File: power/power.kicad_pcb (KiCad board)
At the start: 4 copper layers, 75 x 56 mm, 66 parts, among them J1 GPIO, J10 SCL1, J11 SDA1, J12 SCL2, J13 SDA2, J14 VCC1, J15 GND1, J16 VCC2, J17 GND2, J18 JP_VCC_PWM, J19 Conn_01x01, J2 PWM_OUT, J3 PWM_IN, J4 JP_EXT, J5 JP_VOLTS, J6 I2C_EXT1, J7 I2C_EXT2, J8 PWM_OUT, J9 JP_VCC_PWM, Q1 D15P05, Q2 BC847C, U2 REF5050IDGK, U3 L78L06_SOT89, U5 TPS56A37RPAR

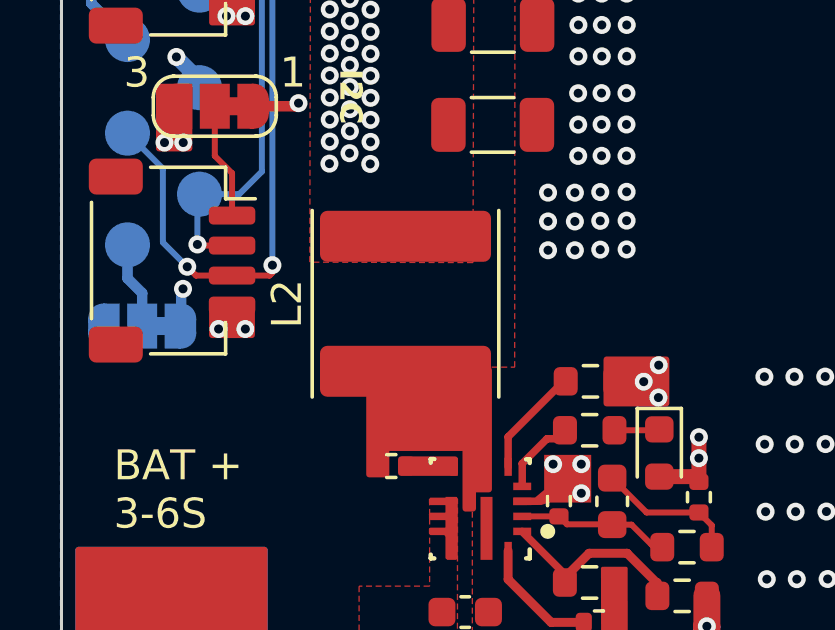
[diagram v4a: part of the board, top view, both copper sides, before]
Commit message: add custom inductor footprint
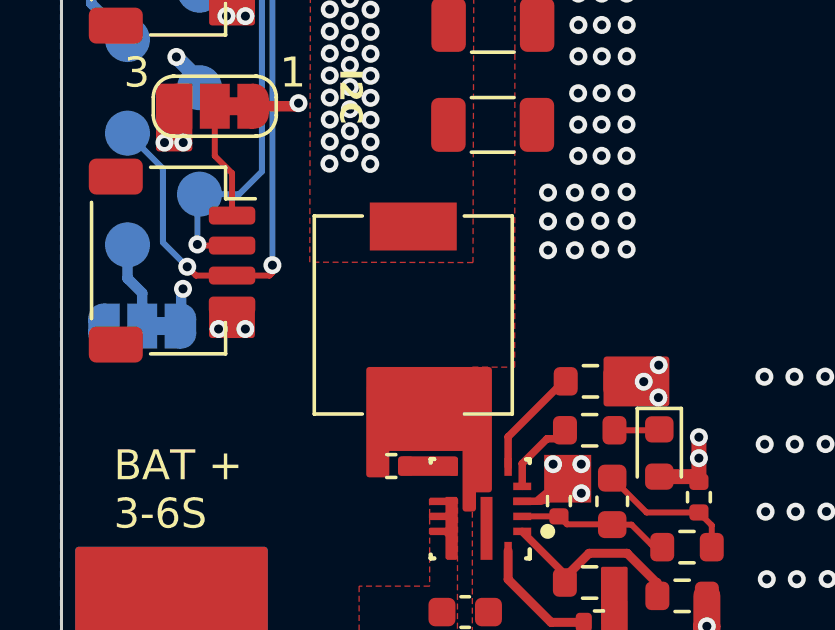
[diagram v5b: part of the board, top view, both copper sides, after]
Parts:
- L2: footprint Inductor_SMD:L_Sunlord_SWPA6045S -> pilotpi:L_6.6x7.5_H4
- moved L2 0.45 mm to (111.7, 69.8)
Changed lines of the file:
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@@
 		)
 	)
-	(footprint "Inductor_SMD:L_Sunlord_SWPA6045S"
+	(footprint "pilotpi:L_6.6x7.5_H4"
 		(layer "F.Cu")
-		(at 111.466844 69.437848 90)
-		(descr "Inductor, Sunlord, SWPA6045S, 6.0x6.0x4.5mm, (https://www.sunlordinc.com/UploadFiles/PDF_Cat/20120704094224784.pdf)")
-		(tags "swpa")
+		(at 111.726498 69.811381 90)
+		(descr "Choke, SMD, 6.3x6.3mm 3mm height")
+		(tags "Choke SMD")
 		(property "Reference" "L2"
-			(at 0 -3.95 90)
-			(layer "F.SilkS")
+			(at 0 -4.45 90)
+			(layer "F.SilkS")
+			(hide yes)
 			(effects
 				(font
@@
 		)
 		(property "Value" "3.3uH 16A 6.5mΩ ±20%"
-			(at 0 3.95 90)
+			(at 0 4.45 90)
 			(layer "F.Fab")
 			(effects
@@
 		(property "Datasheet" ""
 			(at 0 0 90)
+			(unlocked yes)
 			(layer "F.Fab")
 			(hide yes)
@@
 				(font
 					(size 1.27 1.27)
+					(thickness 0.15)
 				)
 			)
@@
 		(property "Description" "I_peak = 11.25A, I_rms = 10.03A"
 			(at 0 0 90)
+			(unlocked yes)
 			(layer "F.Fab")
 			(hide yes)
@@
 				(font
 					(size 1.27 1.27)
-				)
-			)
-		)
-		(property "KiLib_Generator" "inductor/SMD"
-			(at 0 0 90)
-			(layer "F.SilkS")
-			(hide yes)
-			(effects
-				(font
-					(size 1 1)
 					(thickness 0.15)
 				)
@@
 		(duplicate_pad_numbers_are_jumpers no)
 		(fp_line
-			(start -3.11 -3.11)
-			(end 3.11 -3.11)
-			(stroke
-				(width 0.12)
-				(type solid)
-			)
-			(layer "F.SilkS")
-		)
-		(fp_line
-			(start 3.11 3.11)
-			(end -3.11 3.11)
-			(stroke
-				(width 0.12)
-				(type solid)
-			)
-			(layer "F.SilkS")
-		)
-		(fp_line
-			(start 3.25 -3.25)
-			(end 3.25 -3.1)
-			(stroke
-				(width 0.05)
-				(type solid)
-			)
-			(layer "F.CrtYd")
-		)
-		(fp_line
-			(start -3.25 -3.25)
-			(end 3.25 -3.25)
-			(stroke
-				(width 0.05)
-				(type solid)
-			)
-			(layer "F.CrtYd")
-		)
-		(fp_line
-			(start 3.35 -3.1)
-			(end 3.35 3.1)
-			(stroke
-				(width 0.05)
-				(type solid)
-			)
-			(layer "F.CrtYd")
-		)
-		(fp_line
-			(start 3.25 -3.1)
-			(end 3.35 -3.1)
-			(stroke
-				(width 0.05)
-				(type solid)
-			)
-			(layer "F.CrtYd")
-		)
-		(fp_line
-			(start -3.25 -3.1)
-			(end -3.25 -3.25)
-			(stroke
-				(width 0.05)
-				(type solid)
-			)
-			(layer "F.CrtYd")
-		)
-		(fp_line
-			(start -3.35 -3.1)
-			(end -3.25 -3.1)
-			(stroke
-				(width 0.05)
-				(type solid)
-			)
-			(layer "F.CrtYd")
-		)
-		(fp_line
-			(start 3.35 3.1)
-			(end 3.25 3.1)
-			(stroke
-				(width 0.05)
-				(type solid)
-			)
-			(layer "F.CrtYd")
-		)
-		(fp_line
-			(start 3.25 3.1)
-			(end 3.25 3.25)
-			(stroke
-				(width 0.05)
-				(type solid)
-			)
-			(layer "F.CrtYd")
-		)
-		(fp_line
-			(start -3.25 3.1)
-			(end -3.35 3.1)
-			(stroke
-				(width 0.05)
-				(type solid)
-			)
-			(layer "F.CrtYd")
-		)
-		(fp_line
-			(start -3.35 3.1)
-			(end -3.35 -3.1)
-			(stroke
-				(width 0.05)
-				(type solid)
-			)
-			(layer "F.CrtYd")
-		)
-		(fp_line
-			(start 3.25 3.25)
-			(end -3.25 3.25)
-			(stroke
-				(width 0.05)
-				(type solid)
-			)
-			(layer "F.CrtYd")
-		)
-		(fp_line
-			(start -3.25 3.25)
-			(end -3.25 3.1)
-			(stroke
-				(width 0.05)
-				(type solid)
-			)
-			(layer "F.CrtYd")
-		)
-		(fp_rect
-			(start -3 -3)
-			(end 3 3)
-			(stroke
-				(width 0.1)
-				(type solid)
-			)
-			(fill no)
+			(start 3.3 -3.3)
+			(end 3.3 -1.7)
+			(stroke
+				(width 0.12)
+				(type solid)
+			)
+			(layer "F.SilkS")
+		)
+		(fp_line
+			(start -3.3 -3.3)
+			(end 3.3 -3.3)
+			(stroke
+				(width 0.12)
+				(type solid)
+			)
+			(layer "F.SilkS")
+		)
+		(fp_line
+			(start -3.3 -1.7)
+			(end -3.3 -3.3)
+			(stroke
+				(width 0.12)
+				(type solid)
+			)
+			(layer "F.SilkS")
+		)
+		(fp_line
+			(start 3.3 1.7)
+			(end 3.3 3.3)
+			(stroke
+				(width 0.12)
+				(type solid)
+			)
+			(layer "F.SilkS")
+		)
+		(fp_line
+			(start 3.3 3.3)
+			(end -3.3 3.3)
+			(stroke
+				(width 0.12)
+				(type solid)
+			)
+			(layer "F.SilkS")
+		)
+		(fp_line
+			(start -3.3 3.3)
+			(end -3.3 1.7)
+			(stroke
+				(width 0.12)
+				(type solid)
+			)
+			(layer "F.SilkS")
+		)
+		(fp_line
+			(start 3.75 -3.4)
+			(end -3.75 -3.4)
+			(stroke
+				(width 0.05)
+				(type solid)
+			)
+			(layer "F.CrtYd")
+		)
+		(fp_line
+			(start -3.75 -3.4)
+			(end -3.75 3.4)
+			(stroke
+				(width 0.05)
+				(type solid)
+			)
+			(layer "F.CrtYd")
+		)
+		(fp_line
+			(start 3.75 3.4)
+			(end 3.75 -3.4)
+			(stroke
+				(width 0.05)
+				(type solid)
+			)
+			(layer "F.CrtYd")
+		)
+		(fp_line
+			(start -3.75 3.4)
+			(end 3.75 3.4)
+			(stroke
+				(width 0.05)
+				(type solid)
+			)
+			(layer "F.CrtYd")
+		)
+		(fp_line
+			(start 3.15 -3.15)
+			(end 3.15 -1.5)
+			(stroke
+				(width 0.1)
+				(type solid)
+			)
+			(layer "F.Fab")
+		)
+		(fp_line
+			(start -3.15 -3.15)
+			(end 3.15 -3.15)
+			(stroke
+				(width 0.1)
+				(type solid)
+			)
+			(layer "F.Fab")
+		)
+		(fp_line
+			(start -3.15 -3.15)
+			(end -3.15 -1.5)
+			(stroke
+				(width 0.1)
+				(type solid)
+			)
+			(layer "F.Fab")
+		)
+		(fp_line
+			(start 3.15 3.15)
+			(end 3.15 1.5)
+			(stroke
+				(width 0.1)
+				(type solid)
+			)
+			(layer "F.Fab")
+		)
+		(fp_line
+			(start -3.15 3.15)
+			(end -3.15 1.5)
+			(stroke
+				(width 0.1)
+				(type solid)
+			)
+			(layer "F.Fab")
+		)
+		(fp_line
+			(start -3.15 3.15)
+			(end 3.15 3.15)
+			(stroke
+				(width 0.1)
+				(type solid)
+			)
+			(layer "F.Fab")
+		)
+		(fp_arc
+			(start -1.91 -1.91)
+			(mid 0 -2.701148)
+			(end 1.91 -1.91)
+			(stroke
+				(width 0.1)
+				(type solid)
+			)
+			(layer "F.Fab")
+		)
+		(fp_arc
+			(start 1.91 1.91)
+			(mid 0 2.701148)
+			(end -1.91 1.91)
+			(stroke
+				(width 0.1)
+				(type solid)
+			)
 			(layer "F.Fab")
 		)
@@
 			)
 		)
-		(pad "1" smd roundrect
-			(at -2.25 0 90)
-			(size 1.7 5.7)
+		(pad "1" smd rect
+			(at -2.95 0 90)
+			(size 1.6 2.9)
 			(layers "F.Cu" "F.Mask" "F.Paste")
-			(roundrect_rratio 0.147059)
 			(net "Net-(U5-SW)")
 			(pinfunction "1_1")
 			(pintype "passive")
 		)
-		(pad "2" smd roundrect
-			(at 2.25 0 90)
-			(size 1.7 5.7)
+		(pad "2" smd rect
+			(at 2.95 0 90)
+			(size 1.6 2.9)
 			(layers "F.Cu" "F.Mask" "F.Paste")
-			(roundrect_rratio 0.147059)
 			(net "+5V")
 			(pinfunction "2_2")
@@
 		)
 		(embedded_fonts no)
-		(model "${KICAD10_3DMODEL_DIR}/Inductor_SMD.3dshapes/L_Sunlord_SWPA6045S.step"
+		(model "${KICAD10_3DMODEL_DIR}/Inductor_SMD.3dshapes/L_6.3x6.3_H3.step"
 			(offset
 				(xyz 0 0 0)

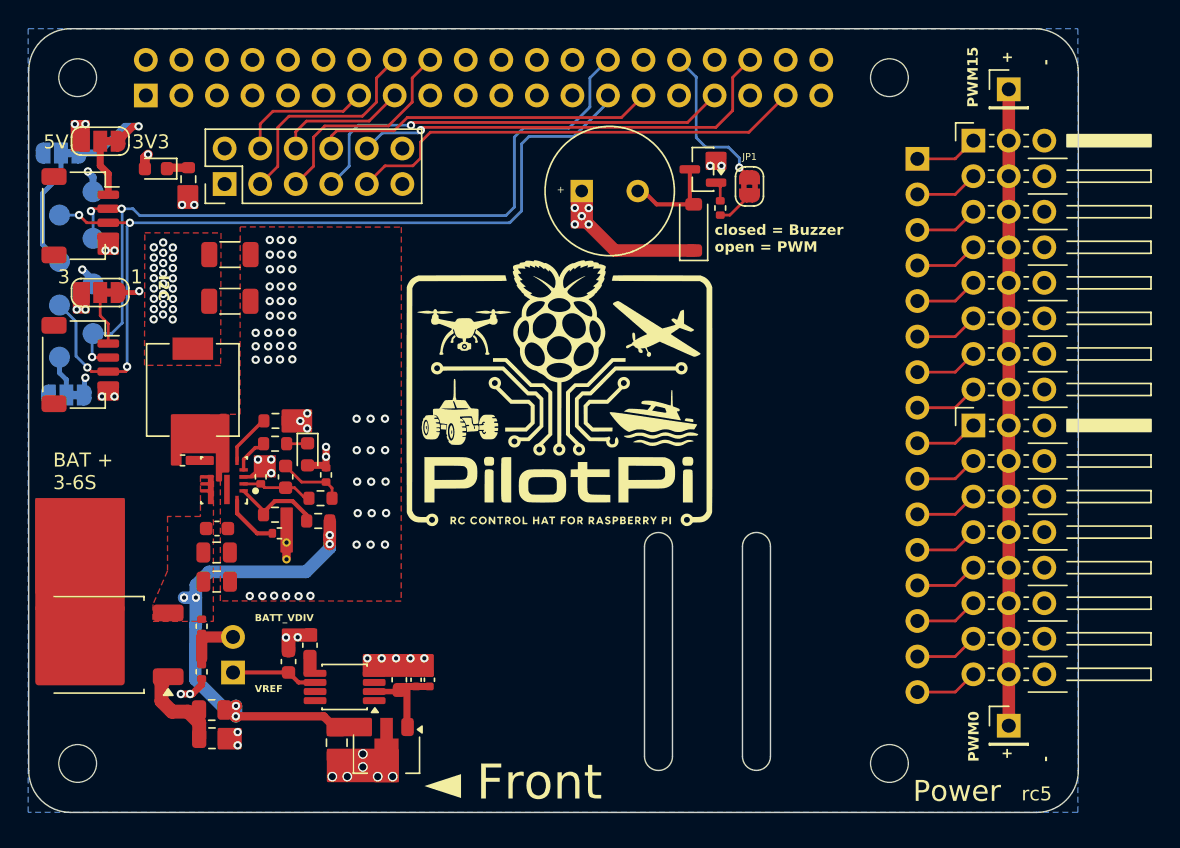
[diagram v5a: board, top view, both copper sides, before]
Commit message: added RGB indicator LED w/LP5562; added I2C pullups
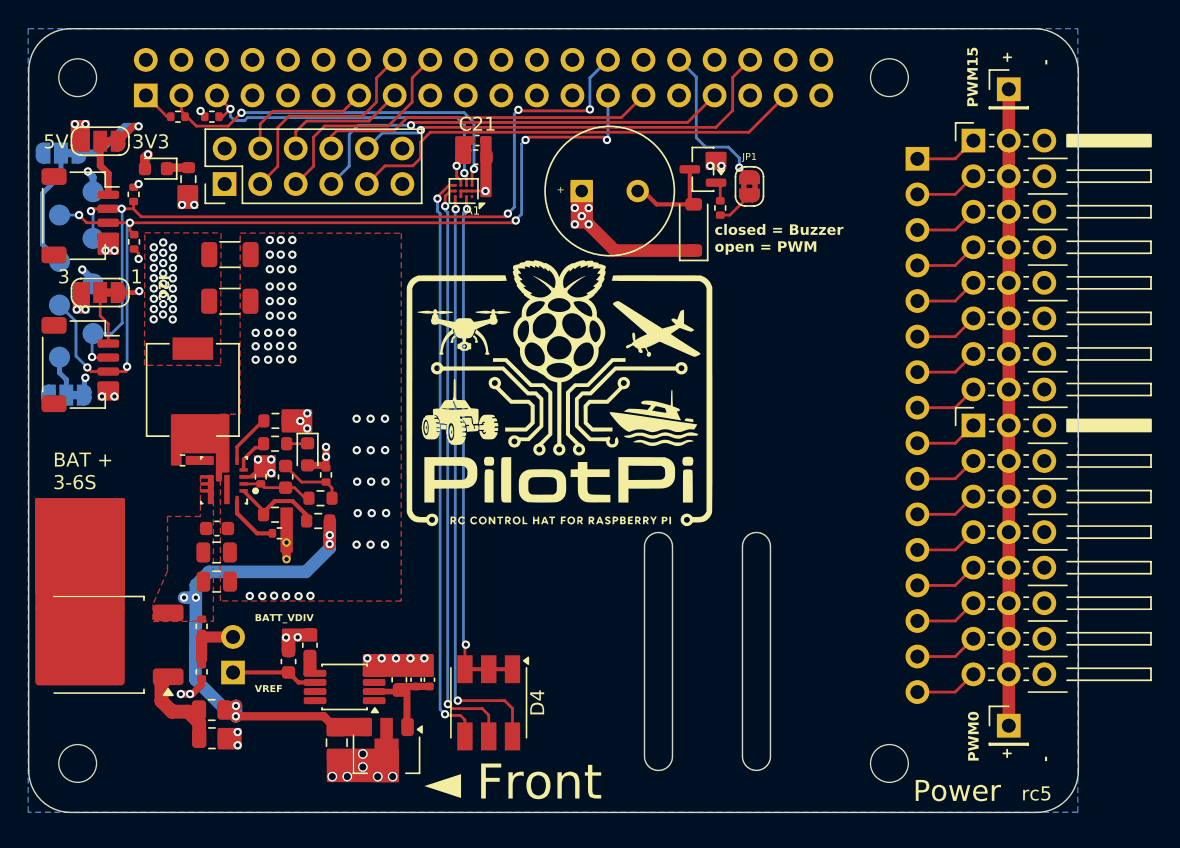
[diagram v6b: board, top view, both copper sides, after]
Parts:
- added C21: 100nF (104) 10% 16V, Capacitor_SMD:C_0402_1005Metric, F.Cu at (132.1, 52.0)
- added C22: 1uF (105) 10% 50V, Capacitor_SMD:C_0603_1608Metric, F.Cu at (131.9, 53.2)
- added D4: LED_RGB, LED_SMD:LED_RGB_5050-6, F.Cu at (132.9, 92.2)
- added R33: 3.3KΩ ±1%, Resistor_SMD:R_0402_1005Metric, F.Cu at (107.5, 59.2)
- added R34: 3.3KΩ ±1%, Resistor_SMD:R_0402_1005Metric, F.Cu at (107.5, 55.8)
- added R35: 3.3KΩ ±1%, Resistor_SMD:R_0402_1005Metric, F.Cu at (110.7, 50.3)
- added R36: 3.3KΩ ±1%, Resistor_SMD:R_0402_1005Metric, F.Cu at (113.1, 50.3)
- added U1: LP5562, pilotpi:Texas_DSBGA-12_1.648x1.248mm_Layout3x4_P0.4mm, F.Cu at (131.1, 55.6)
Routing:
- net +3V3: track 60.7 -> 117.7 mm, vias 3 -> 9
- net Net-(D4-RA): track 0.00 -> 42.2 mm, vias 0 -> 2
- net Net-(D4-GA): track 0.00 -> 42.0 mm, vias 0 -> 2
- net Net-(D4-BA): track 0.00 -> 41.6 mm, vias 0 -> 2
- net /GPIO2/SDA1: track 0.00 -> 27.7 mm, vias 0 -> 2
- net /GPIO3/SCL1: track 0.00 -> 24.5 mm, vias 0 -> 2
- net /GPIO0/SDA0: track 64.8 -> 68.2 mm, vias 4 -> 7
- net GND: track 5.56 -> 7.72 mm, vias 78 -> 79
- net /GPIO1/SCL0: track 61.8 -> 63.5 mm, vias 3 -> 6

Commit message: change UVLO network Better protect against reverse current outrush when disconnecting the battery with external 5V supply connected. -> VSTART=7.96V, VSTOP=7.16, hysteresis=797mV (s. https://www.ti.com/lit/ds/symlink/tps56a37.pdf?ts=1779344700851 Chapter 6.3.6)
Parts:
- R13: value 169kΩ / 1% -> 17.8kΩ / 1%
- R14: value 36.1kΩ / 1% -> 3.09kΩ / 1%
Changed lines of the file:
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@@
 			)
 		)
-		(property "Value" "169kΩ / 1%"
+		(property "Value" "17.8kΩ / 1%"
 			(at 0 1.43 0)
 			(layer "F.Fab")
@@
 			)
 		)
-		(property "Part" "0603WAF1693T5E"
+		(property "Part" "PTFR0402B17K8N9"
 			(at 0 0 0)
 			(unlocked yes)
@@
 			)
 		)
-		(property "Value" "36.1kΩ / 1%"
+		(property "Value" "3.09kΩ / 1%"
 			(at 0 1.43 0)
 			(layer "F.Fab")
@@
 			)
 		)
-		(property "Part" "RT0603BRD0736K1L"
+		(property "Part" "FRC0603F3091TS"
 			(at 0 0 0)
 			(unlocked yes)

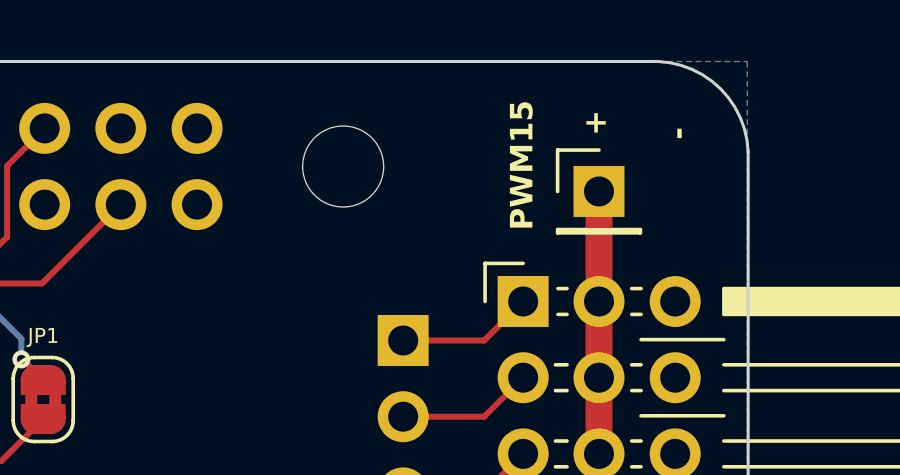
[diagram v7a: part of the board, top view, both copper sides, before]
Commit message: add 5V pin pad near PWM VCC input pin
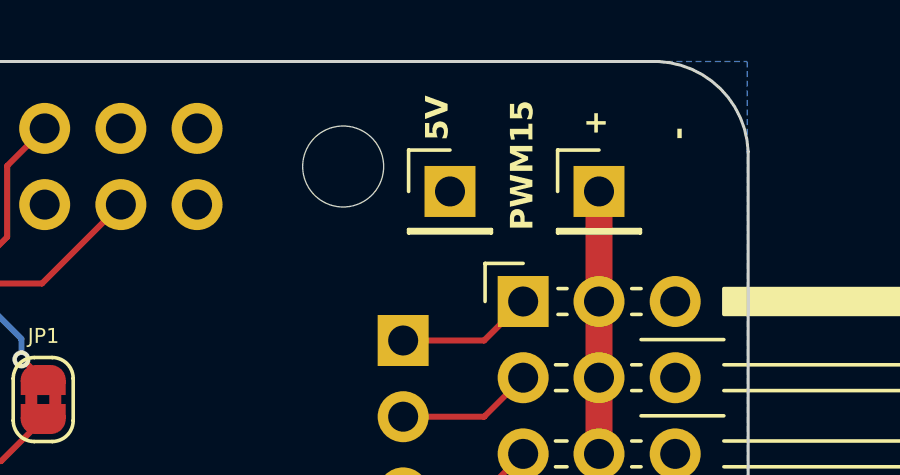
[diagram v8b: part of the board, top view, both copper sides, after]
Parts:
- added J20: JP_VCC_PWM, Connector_PinHeader_2.54mm:PinHeader_1x01_P2.54mm_Vertical, F.Cu at (165.1, 48.3)
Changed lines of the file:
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@@
 		)
 	)
+	(footprint "Connector_PinHeader_2.54mm:PinHeader_1x01_P2.54mm_Vertical"
+		(layer "F.Cu")
+		(at 165.061167 48.332007)
+		(descr "Through hole straight pin header, 1x01, 2.54mm pitch, single row")
+		(tags "Through hole pin header THT 1x01 2.54mm single row")
+		(property "Reference" "J20"
+			(at 0 -2.38 0)
+			(layer "F.SilkS")
+			(hide yes)
+			(effects
+				(font
+					(size 1 1)
+					(thickness 0.15)
+				)
+			)
+		)
+		(property "Value" "JP_VCC_PWM"
+			(at 0 2.38 0)
+			(layer "F.Fab")
+			(effects
+				(font
+					(size 1 1)
+					(thickness 0.15)
+				)
+			)
+		)
+		(property "Datasheet" ""
+			(at 0 0 0)
+			(layer "F.Fab")
+			(hide yes)
+			(effects
+				(font
+					(size 1.27 1.27)
+				)
+			)
+		)
+		(property "Description" "Generic connector, single row, 01x01, script generated (kicad-library-utils/schlib/autogen/connector/)"
+			(at 0 0 0)
+			(layer "F.Fab")
+			(hide yes)
+			(effects
+				(font
+					(size 1.27 1.27)
+				)
+			)
+		)
+		(property "KiLib_Generator" "connector/pin_header_socket"
+			(at 0 0 0)
+			(layer "F.SilkS")
+			(hide yes)
+			(effects
+				(font
+					(size 1 1)
+					(thickness 0.15)
+				)
+			)
+		)
+		(property "Part" ""
+			(at 0 0 0)
+			(unlocked yes)
+			(layer "F.Fab")
+			(hide yes)
+			(effects
+				(font
+					(size 0.5 1)
+					(thickness 0.125)
+				)
+			)
+		)
+		(property ki_fp_filters "Connector*:*_1x??_*")
+		(sheetname "/")
+		(sheetfile "power.kicad_sch")
+		(units
+			(unit
+				(name "A")
+				(pins "1")
+			)
+		)
+		(attr through_hole exclude_from_pos_files exclude_from_bom)
+		(duplicate_pad_numbers_are_jumpers no)
+		(fp_line
+			(start -1.38 -1.38)
+			(end 0 -1.38)
+			(stroke
+				(width 0.12)
+				(type solid)
+			)
+			(layer "F.SilkS")
+		)
+		(fp_line
+			(start -1.38 0)
+			(end -1.38 -1.38)
+			(stroke
+				(width 0.12)
+				(type solid)
+			)
+			(layer "F.SilkS")
+		)
+		(fp_line
+			(start -1.38 1.27)
+			(end -1.38 1.38)
+			(stroke
+				(width 0.12)
+				(type solid)
+			)
+			(layer "F.SilkS")
+		)
+		(fp_line
+			(start -1.38 1.27)
+			(end 1.38 1.27)
+			(stroke
+				(width 0.12)
+				(type solid)
+			)
+			(layer "F.SilkS")
+		)
+		(fp_line
+			(start -1.38 1.38)
+			(end 1.38 1.38)
+			(stroke
+				(width 0.12)
+				(type solid)
+			)
+			(layer "F.SilkS")
+		)
+		(fp_line
+			(start 1.38 1.27)
+			(end 1.38 1.38)
+			(stroke
+				(width 0.12)
+				(type solid)
+			)
+			(layer "F.SilkS")
+		)
+		(fp_rect
+			(start -1.77 -1.77)
+			(end 1.77 1.77)
+			(stroke
+				(width 0.05)
+				(type solid)
+			)
+			(fill no)
+			(layer "F.CrtYd")
+		)
+		(fp_line
+			(start -1.27 -0.635)
+			(end -0.635 -1.27)
+			(stroke
+				(width 0.1)
+				(type solid)
+			)
+			(layer "F.Fab")
+		)
+		(fp_line
+			(start -1.27 1.27)
+			(end -1.27 -0.635)
+			(stroke
+				(width 0.1)
+				(type solid)
+			)
+			(layer "F.Fab")
+		)
+		(fp_line
+			(start -0.635 -1.27)
+			(end 1.27 -1.27)
+			(stroke
+				(width 0.1)
+				(type solid)
+			)
+			(layer "F.Fab")
+		)
+		(fp_line
+			(start 1.27 -1.27)
+			(end 1.27 1.27)
+			(stroke
+				(width 0.1)
+				(type solid)
+			)
+			(layer "F.Fab")
+		)
+		(fp_line
+			(start 1.27 1.27)
+			(end -1.27 1.27)
+			(stroke
+				(width 0.1)
+				(type solid)
+			)
+			(layer "F.Fab")
+		)
+		(fp_text user "${REFERENCE}"
+			(at 0 0 90)
+			(layer "F.Fab")
+			(effects
+				(font
+					(size 1 1)
+					(thickness 0.15)
+				)
+			)
+		)
+		(pad "1" thru_hole rect
+			(at 0 0)
+			(size 1.7 1.7)
+			(drill 1)
+			(layers "*.Cu" "*.Mask")
+			(remove_unused_layers no)
+			(net "+5V")
+			(pinfunction "Pin_1_1")
+			(pintype "passive")
+		)
+		(embedded_fonts no)
+		(model "${KICAD10_3DMODEL_DIR}/Connector_PinHeader_2.54mm.3dshapes/PinHeader_1x01_P2.54mm_Vertical.step"
+			(offset
+				(xyz 0 0 0)
+			)
+			(scale
+				(xyz 1 1 1)
+			)
+			(rotate
+				(xyz 0 0 0)
+			)
+		)
+	)
 	(footprint "Capacitor_SMD:C_0805_2012Metric"
 		(layer "F.Cu")
@@
 		(layer "F.SilkS")
 		(effects
+			(font
+				(size 0.75 0.75)
+				(thickness 0.125)
+				(bold yes)
+			)
+			(justify left bottom)
+		)
+	)
+	(gr_text "5V"
+		(at 165.07 46.64 90)
+		(layer "F.SilkS")
+		(effects
